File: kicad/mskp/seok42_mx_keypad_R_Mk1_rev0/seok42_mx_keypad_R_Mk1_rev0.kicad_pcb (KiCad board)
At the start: 2 copper layers, 142 x 102 mm, 50 parts, among them J1 Conn_01x12_Socket, SW1 Switch, SW10 Switch, SW11 Switch, SW12 Switch, SW13 Switch, SW14 Switch, SW15 Switch, SW16 Switch, SW17 Switch, SW18 Switch, SW19 Switch, SW2 Switch, SW20 Switch, SW21 Switch, SW3 Switch, SW4 Switch, SW5 Switch, SW6 Switch, SW7 Switch, SW8 Switch, SW9 Switch

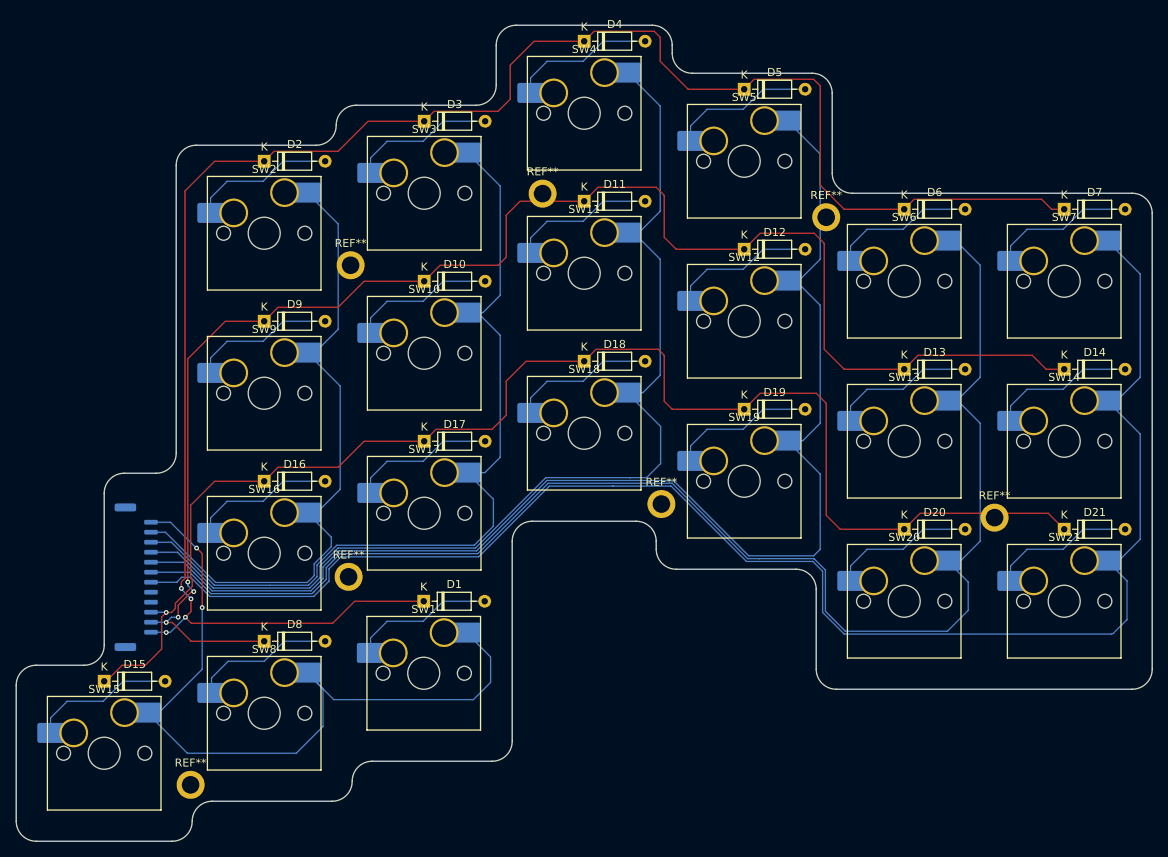
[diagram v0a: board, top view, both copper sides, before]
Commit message: Adds silkscreen for seok42_mx_keypad_R_Mk1_rev0 PCB
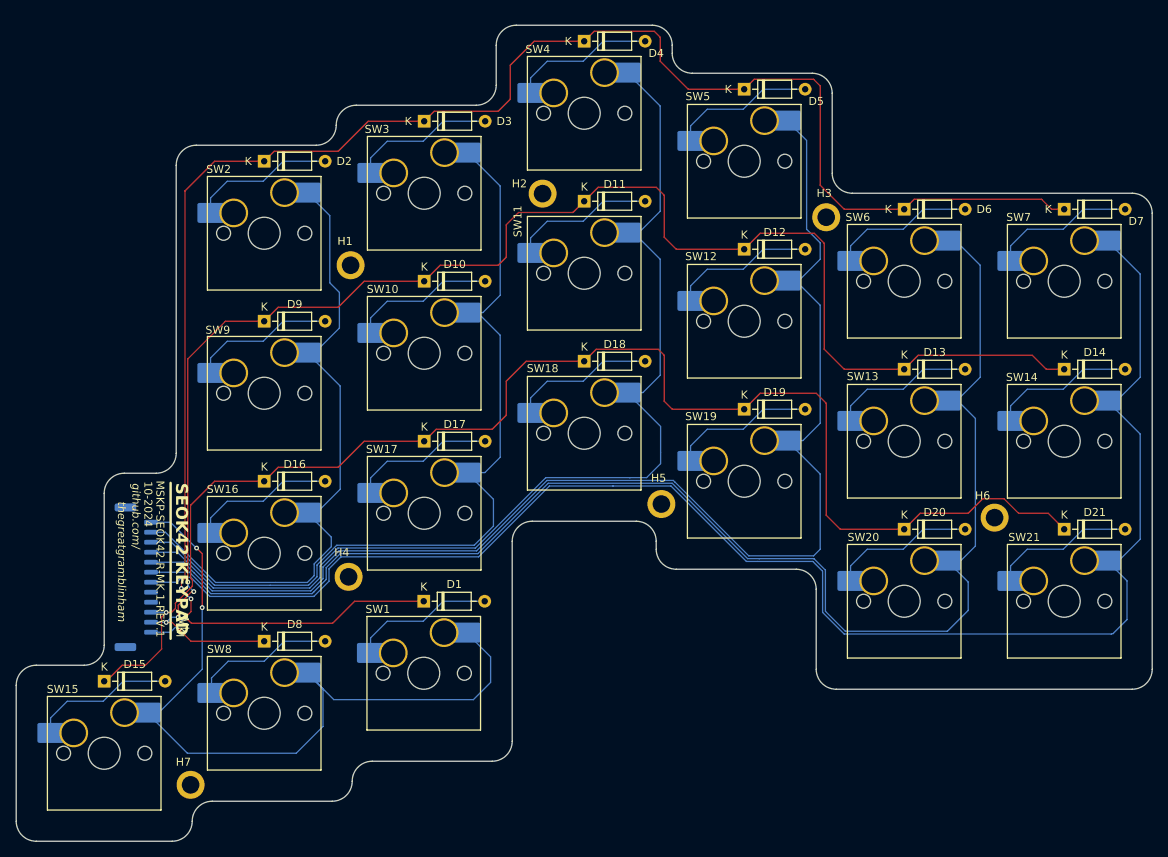
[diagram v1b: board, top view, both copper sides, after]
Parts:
- renumbered REF** to H1, REF** to H2, REF** to H3, REF** to H4, REF** to H5, REF** to H6, REF** to H7
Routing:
- net Net-(D15-K): track 174.8 -> 176.3 mm
- net Net-(D10-K): track 195.4 -> 194.6 mm
- net Net-(D1-K): vias 4 -> 3
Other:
- board text added: "10-2024"
- board text added: "CONTROL BOARD"
- board text added: "I"
- board text added: "MSKP-SEOK42-R-MK.1-REV.1"
- board text added: "Mk"
- board text added: "SEOK42 KEYPAD"
- board text added: "SW1"
- board text added: "SW10"
- board text added: "SW11"
- board text added: "SW12"
- board text added: "SW13"
- board text added: "SW14"
- board text added: "SW15"
- board text added: "SW16"
- board text added: "SW17"
- board text added: "SW18"
- board text added: "SW19"
- board text added: "SW2"
- board text added: "SW20"
- board text added: "SW21"
- board text added: "SW3"
- board text added: "SW4"
- board text added: "SW5"
- board text added: "SW6"
- board text added: "SW7"
- board text added: "SW8"
- board text added: "SW9"
- board text added: "github.com/"
- board text added: "thegreatgramblinham"

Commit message: Final tweaks to PCBs before second round of mskp fabrications
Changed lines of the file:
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@@
 			(plot_on_all_layers_selection 0x0000000_00000000)
 			(disableapertmacros no)
-			(usegerberextensions no)
-			(usegerberattributes yes)
-			(usegerberadvancedattributes yes)
-			(creategerberjobfile yes)
+			(usegerberextensions yes)
+			(usegerberattributes no)
+			(usegerberadvancedattributes no)
+			(creategerberjobfile no)
 			(dashed_line_dash_ratio 12.000000)
 			(dashed_line_gap_ratio 3.000000)
 			(svgprecision 4)
 			(plotframeref no)
-			(viasonmask no)
+			(viasonmask yes)
 			(mode 1)
 			(useauxorigin no)
@@
 			(psa4output no)
 			(plotreference yes)
-			(plotvalue yes)
+			(plotvalue no)
 			(plotfptext yes)
 			(plotinvisibletext no)
 			(sketchpadsonfab no)
-			(subtractmaskfromsilk no)
+			(subtractmaskfromsilk yes)
 			(outputformat 1)
 			(mirror no)
-			(drillshape 1)
+			(drillshape 0)
 			(scaleselection 1)
-			(outputdirectory "")
+			(outputdirectory "seok42_r_mk1_exports")
 		)
 	)
@@
 	)
 	(segment
-		(start 159.75 98.55)
-		(end 159.65 98.55)
-		(width 0.15)
-		(layer "B.Cu")
-		(net 25)
-	)
-	(segment
 		(start 140.4 107.35)
 		(end 123.215076 107.35)
@@
 	)
 	(segment
-		(start 157.65 99.6)
-		(end 157.55 99.6)
-		(width 0.15)
-		(layer "B.Cu")
-		(net 28)
-	)
-	(segment
 		(start 221.85 111.45)
 		(end 221.85 116.3)
@@
 		(width 0.15)
 		(layer "B.Cu")
-		(net 29)
-	)
-	(segment
-		(start 175.9 108.675)
-		(end 175.825 108.675)
-		(width 0.15)
-		(layer "B.Cu")
